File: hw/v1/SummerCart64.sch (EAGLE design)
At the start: 85 parts, among them J1 N64_EDGE, J2 molex 104031-0811, J3 10118192-0002LF, J4 SSW-106-02-G-D, U1 10M08SCE144C8G, U10 AZ1117IH-3.3TRG1, U2 IS42S16320F-7TL, U3 ATTINY45-20XU, U4 W25Q128JVSIM, U5 IS62WVS2568GBLL-45NLI, U6 AT93C66B-XHM, U7 SN74LVC125APWR, U8 MCP7940NT-I/ST, U9 FT2232HL, X1 XLH336050.000000I, X2 FC-12M 32.7680KA-AC3, X3 XLH336012.000000X

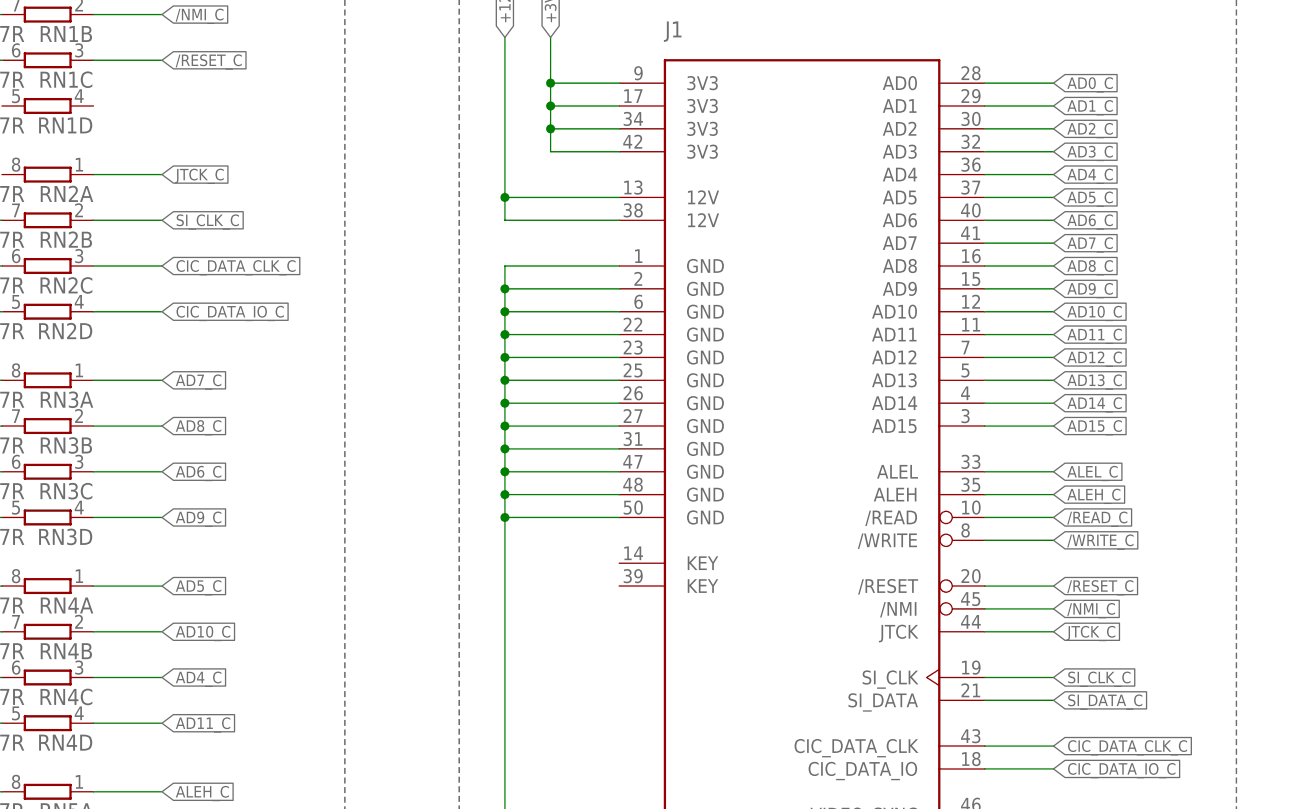
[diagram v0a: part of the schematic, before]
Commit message: device_arbiter overhaul, ddipl stuff added
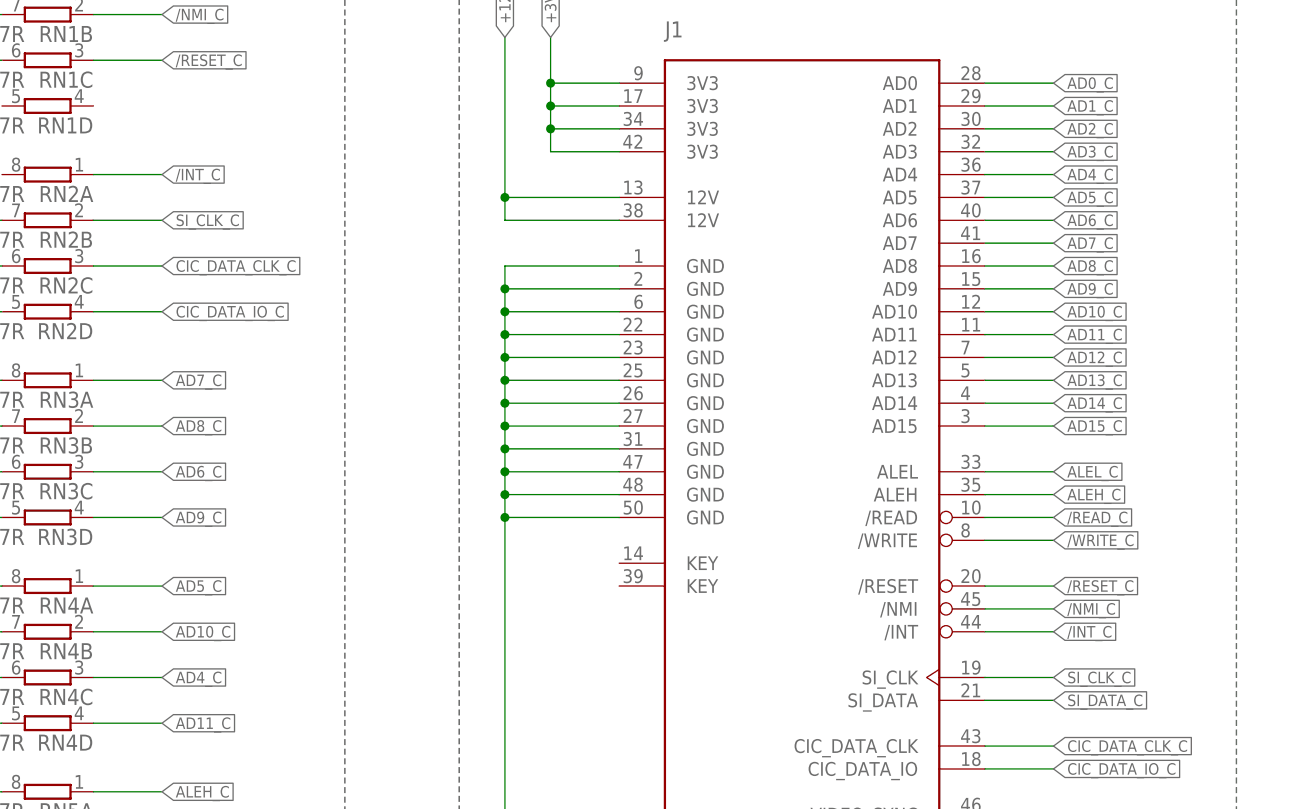
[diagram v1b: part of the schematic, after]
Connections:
- removed net JTCK_C: J1.JTCK, RN2A.1
- new net /INT_C: J1./INT, RN2A.1
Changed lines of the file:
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@@
-</segment>
-</net>
-<net name="JTCK_C" class="0">
-<segment>
-<pinref part="J1" gate="&gt;NAME" pin="JTCK"/>
-<wire x1="274.32" y1="287.02" x2="281.94" y2="287.02" width="0.1524" layer="91"/>
-<label x="281.94" y="287.02" size="1.27" layer="95" xref="yes"/>
-</segment>
-<segment>
-<pinref part="RN2" gate="A" pin="1"/>
-<wire x1="175.26" y1="337.82" x2="182.88" y2="337.82" width="0.1524" layer="91"/>
-<label x="182.88" y="337.82" size="1.27" layer="95" rot="MR180" xref="yes"/>
 </segment>
 </net>
@@
 </segment>
 </net>
+<net name="/INT_C" class="0">
+<segment>
+<pinref part="J1" gate="&gt;NAME" pin="/INT"/>
+<wire x1="274.32" y1="287.02" x2="281.94" y2="287.02" width="0.1524" layer="91"/>
+<label x="281.94" y="287.02" size="1.27" layer="95" xref="yes"/>
+</segment>
+<segment>
+<pinref part="RN2" gate="A" pin="1"/>
+<wire x1="175.26" y1="337.82" x2="182.88" y2="337.82" width="0.1524" layer="91"/>
+<label x="182.88" y="337.82" size="1.27" layer="95" rot="MR180" xref="yes"/>
+</segment>
+</net>
